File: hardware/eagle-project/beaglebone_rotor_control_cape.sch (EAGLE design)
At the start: 26 parts, among them IC1 TLC2264CDU, IC2 TLV5616, IC3 MAX3232ESE, Q1 SQ2348ES-T1-GE3, Q2 SQ2348ES-T1-GE3, X1 BEAGLEBONE_OUTLINE

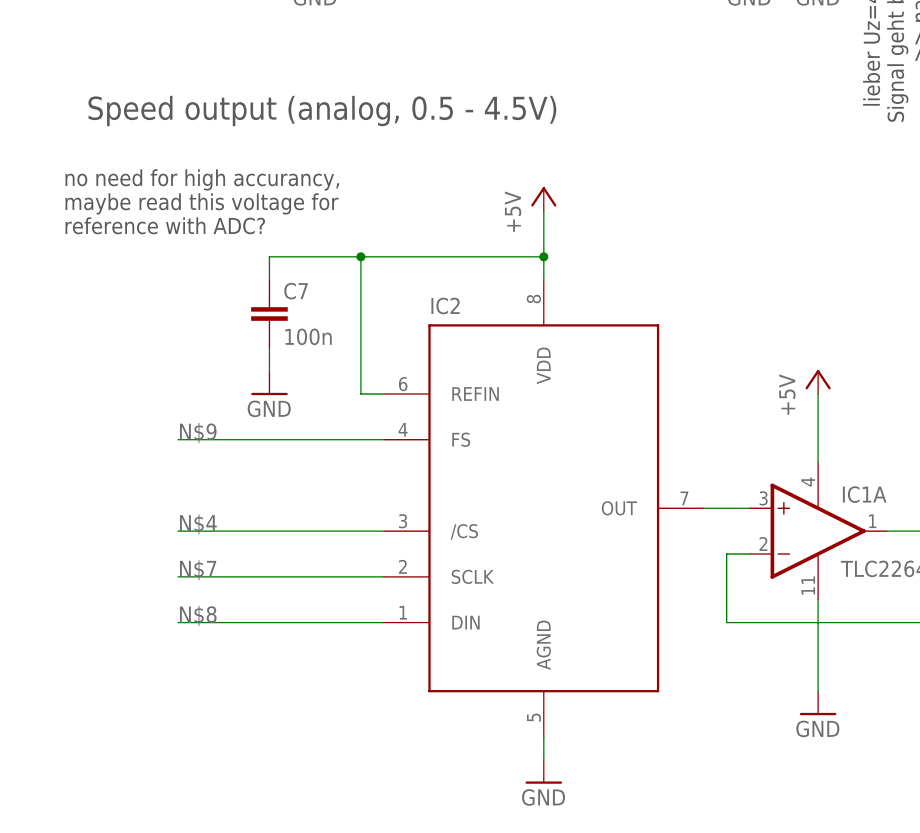
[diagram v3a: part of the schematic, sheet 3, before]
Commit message: Changed DAC from TI TLV5616 to Microchip MCP4901
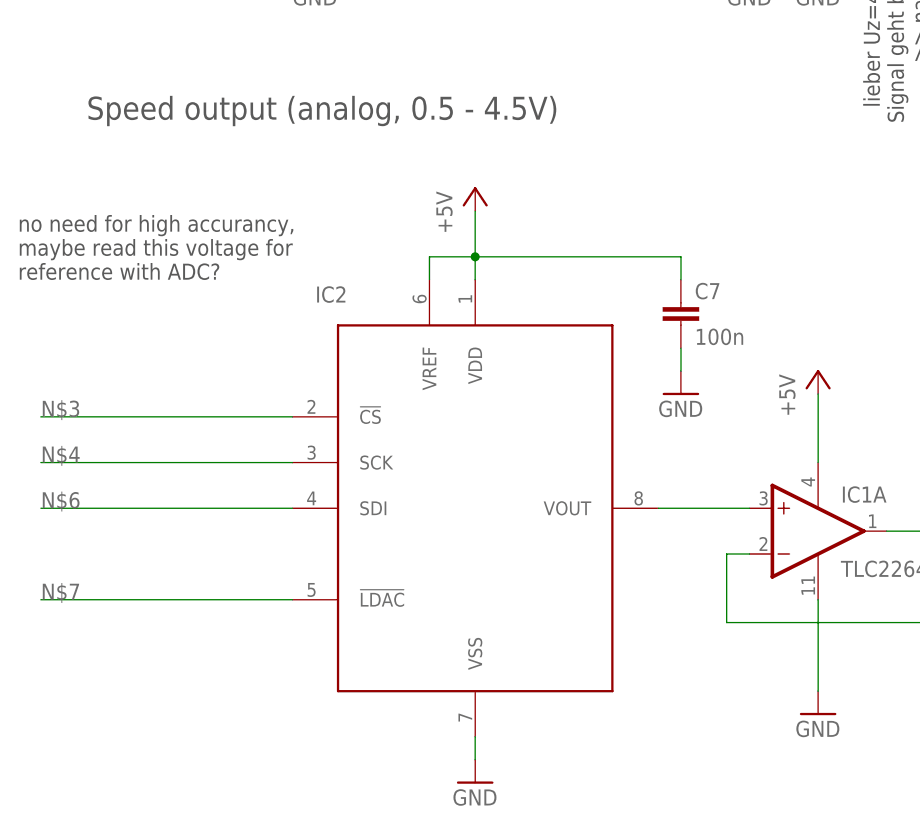
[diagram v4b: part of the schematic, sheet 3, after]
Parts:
- IC2: value TLV5616 -> MCP4901; device ti-tlv5616:TLV5616 -> microchip_mcp4901:MCP4901
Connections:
- removed net N$8: IC2.DIN
- removed net N$9: IC2.FS
- new net N$3: IC2.!CS
- new net N$6: IC2.SDI
- net +5V: now also IC2.VREF; no longer IC2.REFIN
- net GND: now also IC2.VSS; no longer IC2.AGND
- net N$2: now also IC2.VOUT; no longer IC2.OUT
- net N$4: now also IC2.SCK; no longer IC2./CS
- net N$7: now also IC2.!LDAC; no longer IC2.SCLK
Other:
- moved on the sheet: C7, IC2
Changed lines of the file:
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@@
 <part name="GND10" library="supply1" deviceset="GND" device=""/>
 <part name="P+1" library="supply1" deviceset="+5V" device=""/>
-<part name="IC2" library="ti-tlv5616" deviceset="TLV5616" device=""/>
 <part name="P+2" library="supply1" deviceset="+5V" device=""/>
 <part name="GND11" library="supply1" deviceset="GND" device=""/>
@@
 <part name="GND17" library="supply1" deviceset="GND" device=""/>
 <part name="GND18" library="supply1" deviceset="GND" device=""/>
+<part name="IC2" library="microchip_mcp4901" deviceset="MCP4901" device=""/>
 </parts>
 <sheets>
@@
 &gt;&gt; nachmessen!</text>
 <text x="76.2" y="116.84" size="1.778" layer="97">Vcc=5V</text>
-<text x="17.78" y="76.2" size="1.778" layer="97">no need for high accurancy,
+<text x="12.7" y="71.12" size="1.778" layer="97">no need for high accurancy,
 maybe read this voltage for
 reference with ADC?</text>
@@
 <instance part="GND10" gate="1" x="101.6" y="22.86"/>
 <instance part="P+1" gate="1" x="101.6" y="60.96"/>
-<instance part="IC2" gate="G$1" x="71.12" y="45.72"/>
-<instance part="P+2" gate="1" x="71.12" y="81.28"/>
-<instance part="GND11" gate="1" x="71.12" y="15.24"/>
+<instance part="P+2" gate="1" x="63.5" y="81.28"/>
+<instance part="GND11" gate="1" x="63.5" y="15.24"/>
 <instance part="IC1" gate="B" x="76.2" y="124.46" rot="R180"/>
 <instance part="R10" gate="G$1" x="111.76" y="121.92"/>
@@
 <instance part="R7" gate="G$1" x="177.8" y="96.52"/>
 <instance part="R6" gate="G$1" x="175.26" y="147.32"/>
-<instance part="C7" gate="G$1" x="40.64" y="68.58"/>
-<instance part="GND17" gate="1" x="40.64" y="58.42"/>
+<instance part="C7" gate="G$1" x="86.36" y="68.58"/>
+<instance part="GND17" gate="1" x="86.36" y="58.42"/>
 <instance part="GND18" gate="1" x="231.14" y="45.72"/>
+<instance part="IC2" gate="G$1" x="63.5" y="45.72"/>
 </instances>
 <busses>
@@
 </segment>
 <segment>
-<pinref part="IC2" gate="G$1" pin="AGND"/>
 <pinref part="GND11" gate="1" pin="GND"/>
-<wire x1="71.12" y1="17.78" x2="71.12" y2="20.32" width="0.1524" layer="91"/>
+<wire x1="63.5" y1="17.78" x2="63.5" y2="20.32" width="0.1524" layer="91"/>
+<pinref part="IC2" gate="G$1" pin="VSS"/>
 </segment>
 <segment>
@@
 <pinref part="C7" gate="G$1" pin="2"/>
 <pinref part="GND17" gate="1" pin="GND"/>
-<wire x1="40.64" y1="60.96" x2="40.64" y2="63.5" width="0.1524" layer="91"/>
+<wire x1="86.36" y1="60.96" x2="86.36" y2="63.5" width="0.1524" layer="91"/>
 </segment>
 </net>
@@
 </segment>
 <segment>
+<pinref part="P+2" gate="1" pin="+5V"/>
+<wire x1="63.5" y1="78.74" x2="63.5" y2="73.66" width="0.1524" layer="91"/>
+<pinref part="C7" gate="G$1" pin="1"/>
+<wire x1="63.5" y1="73.66" x2="63.5" y2="71.12" width="0.1524" layer="91"/>
+<wire x1="86.36" y1="71.12" x2="86.36" y2="73.66" width="0.1524" layer="91"/>
+<wire x1="86.36" y1="73.66" x2="63.5" y2="73.66" width="0.1524" layer="91"/>
+<junction x="63.5" y="73.66"/>
 <pinref part="IC2" gate="G$1" pin="VDD"/>
-<pinref part="P+2" gate="1" pin="+5V"/>
-<wire x1="71.12" y1="78.74" x2="71.12" y2="73.66" width="0.1524" layer="91"/>
-<pinref part="C7" gate="G$1" pin="1"/>
-<wire x1="71.12" y1="73.66" x2="71.12" y2="71.12" width="0.1524" layer="91"/>
-<wire x1="40.64" y1="71.12" x2="40.64" y2="73.66" width="0.1524" layer="91"/>
-<wire x1="40.64" y1="73.66" x2="50.8" y2="73.66" width="0.1524" layer="91"/>
-<junction x="71.12" y="73.66"/>
-<pinref part="IC2" gate="G$1" pin="REFIN"/>
-<wire x1="50.8" y1="73.66" x2="71.12" y2="73.66" width="0.1524" layer="91"/>
-<wire x1="53.34" y1="58.42" x2="50.8" y2="58.42" width="0.1524" layer="91"/>
-<wire x1="50.8" y1="58.42" x2="50.8" y2="73.66" width="0.1524" layer="91"/>
-<junction x="50.8" y="73.66"/>
+<pinref part="IC2" gate="G$1" pin="VREF"/>
+<wire x1="58.42" y1="71.12" x2="58.42" y2="73.66" width="0.1524" layer="91"/>
+<wire x1="58.42" y1="73.66" x2="63.5" y2="73.66" width="0.1524" layer="91"/>
 </segment>
 <segment>
@@
 <net name="N$2" class="0">
 <segment>
-<pinref part="IC2" gate="G$1" pin="OUT"/>
-<wire x1="88.9" y1="45.72" x2="93.98" y2="45.72" width="0.1524" layer="91"/>
+<wire x1="83.82" y1="45.72" x2="93.98" y2="45.72" width="0.1524" layer="91"/>
 <pinref part="IC1" gate="A" pin="+IN"/>
-</segment>
-</net>
-<net name="N$4" class="0">
-<segment>
-<pinref part="IC2" gate="G$1" pin="/CS"/>
-<wire x1="53.34" y1="43.18" x2="30.48" y2="43.18" width="0.1524" layer="91"/>
-<label x="30.48" y="43.18" size="1.778" layer="95"/>
-</segment>
-</net>
-<net name="N$7" class="0">
-<segment>
-<pinref part="IC2" gate="G$1" pin="SCLK"/>
-<wire x1="30.48" y1="38.1" x2="53.34" y2="38.1" width="0.1524" layer="91"/>
-<label x="30.48" y="38.1" size="1.778" layer="95"/>
-</segment>
-</net>
-<net name="N$8" class="0">
-<segment>
-<pinref part="IC2" gate="G$1" pin="DIN"/>
-<wire x1="53.34" y1="33.02" x2="30.48" y2="33.02" width="0.1524" layer="91"/>
-<label x="30.48" y="33.02" size="1.778" layer="95"/>
-</segment>
-</net>
-<net name="N$9" class="0">
-<segment>
-<pinref part="IC2" gate="G$1" pin="FS"/>
-<wire x1="53.34" y1="53.34" x2="30.48" y2="53.34" width="0.1524" layer="91"/>
-<label x="30.48" y="53.34" size="1.778" layer="95"/>
+<pinref part="IC2" gate="G$1" pin="VOUT"/>
 </segment>
 </net>
@@
 </segment>
 </net>
+<net name="N$3" class="0">
+<segment>
+<pinref part="IC2" gate="G$1" pin="!CS"/>
+<wire x1="43.18" y1="55.88" x2="15.24" y2="55.88" width="0.1524" layer="91"/>
+<label x="15.24" y="55.88" size="1.778" layer="95"/>
+</segment>
+</net>
+<net name="N$4" class="0">
+<segment>
+<pinref part="IC2" gate="G$1" pin="SCK"/>
+<wire x1="15.24" y1="50.8" x2="43.18" y2="50.8" width="0.1524" layer="91"/>
+<label x="15.24" y="50.8" size="1.778" layer="95"/>
+</segment>
+</net>
+<net name="N$6" class="0">
+<segment>
+<pinref part="IC2" gate="G$1" pin="SDI"/>
+<wire x1="43.18" y1="45.72" x2="15.24" y2="45.72" width="0.1524" layer="91"/>
+<label x="15.24" y="45.72" size="1.778" layer="95"/>
+</segment>
+</net>
+<net name="N$7" class="0">
+<segment>
+<pinref part="IC2" gate="G$1" pin="!LDAC"/>
+<wire x1="15.24" y1="35.56" x2="43.18" y2="35.56" width="0.1524" layer="91"/>
+<label x="15.24" y="35.56" size="1.778" layer="95"/>
+</segment>
+</net>

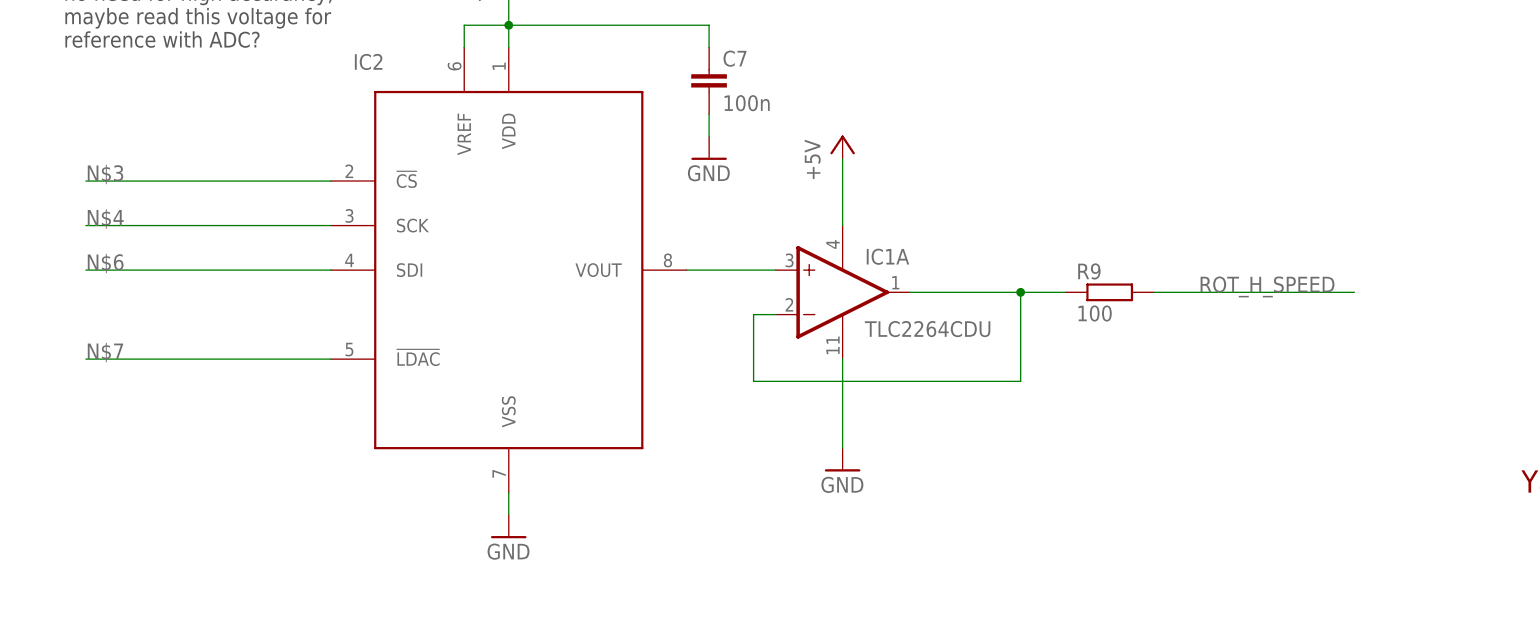
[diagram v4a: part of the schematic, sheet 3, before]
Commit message: Added software draft for MCP4901 and some Eagle schematic updates
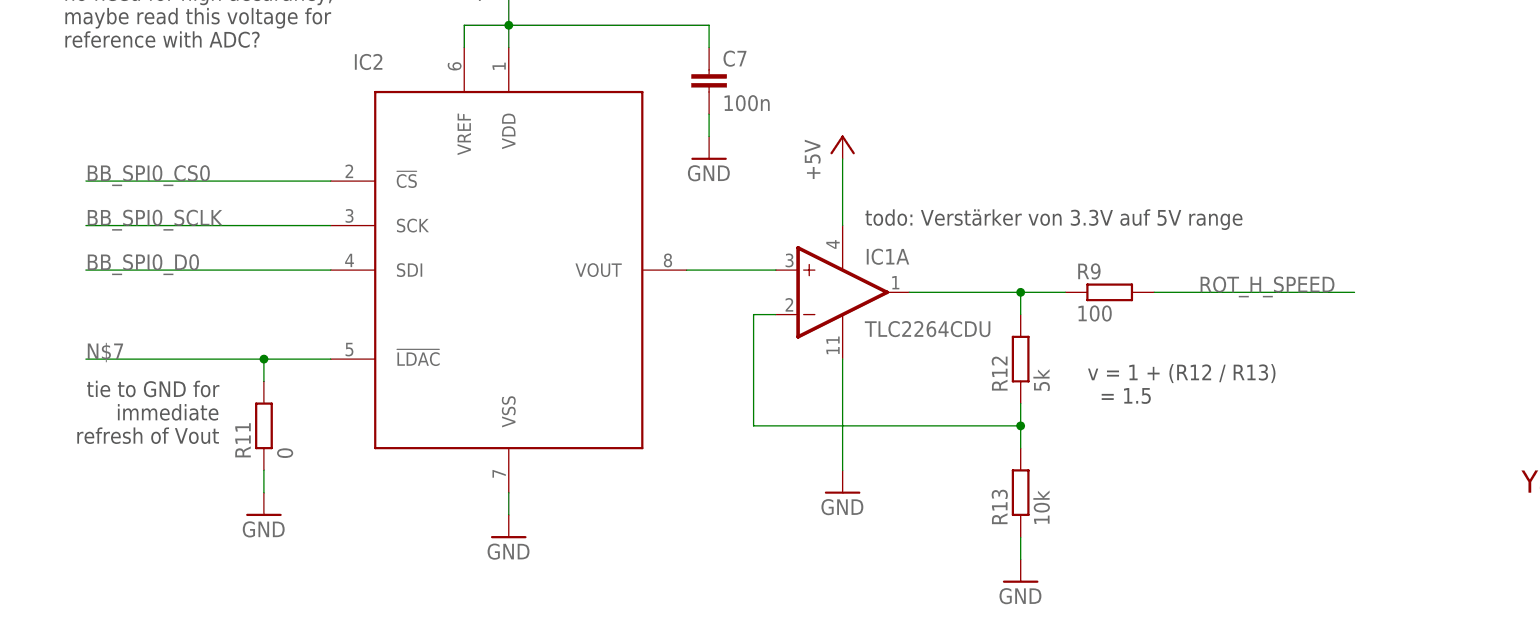
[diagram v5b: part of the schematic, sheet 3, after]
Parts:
- added R11: 0, rcl:R-EU_R0805
- added R12: 5k, rcl:R-EU_R0805
- added R13: 10k, rcl:R-EU_R0805
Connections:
- removed net N$4: IC2.SCK
- removed net N$6: IC2.SDI
- new net BB_SPI0_CS0: IC2.!CS, X1.I2C1_SCL
- new net BB_SPI0_D0: IC2.SDI, X1.UART2_TXD
- new net BB_SPI0_D1: X1.I2C1_SDA
- new net BB_SPI0_SCLK: IC2.SCK, X1.UART2_RXD
- net GND: now also R11.1, R13.1
- net N$3: now also IC1A.OUT, R12.2, R9.1; no longer IC2.!CS
- net N$5: now also R12.1, R13.2; no longer IC1A.OUT, R9.1
- net N$7: now also R11.2
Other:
- note added: "P9.11"
- note added: "P9.13"
- note added: "P9.17"
- note added: "P9.18"
- note added: "P9.21"
- note added: "P9.22"
- note added: "tie to GND for immediate refresh of Vout"
- note added: "todo: Verstärker von 3.3V auf 5V range"
- note added: "v = 1 + (R12 / R13) = 1.5"
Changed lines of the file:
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@@
 <part name="GND18" library="supply1" deviceset="GND" device=""/>
 <part name="IC2" library="microchip_mcp4901" deviceset="MCP4901" device=""/>
+<part name="R11" library="rcl" deviceset="R-EU_" device="R0805" value="0"/>
+<part name="GND19" library="supply1" deviceset="GND" device=""/>
+<part name="R12" library="rcl" deviceset="R-EU_" device="R0805" value="5k"/>
+<part name="R13" library="rcl" deviceset="R-EU_" device="R0805" value="10k"/>
+<part name="GND20" library="supply1" deviceset="GND" device=""/>
 </parts>
 <sheets>
@@
 <text x="147.32" y="152.4" size="2.54" layer="97">Information:</text>
 <text x="147.32" y="142.24" size="1.778" layer="97">- BeagleBone Black cape layout is provided by Adafruit</text>
+<text x="10.16" y="63.5" size="1.778" layer="97">P9.17</text>
+<text x="149.86" y="63.5" size="1.778" layer="97">P9.18</text>
+<text x="149.86" y="58.42" size="1.778" layer="97">P9.22</text>
+<text x="10.16" y="58.42" size="1.778" layer="97">P9.21</text>
+<text x="10.16" y="68.58" size="1.778" layer="97">P9.13</text>
+<text x="10.16" y="71.12" size="1.778" layer="97">P9.11</text>
 </plain>
 <instances>
@@
 <wire x1="22.86" y1="68.58" x2="53.34" y2="68.58" width="0.1524" layer="91"/>
 <label x="22.86" y="68.58" size="1.778" layer="95"/>
+</segment>
+</net>
+<net name="BB_SPI0_CS0" class="0">
+<segment>
+<pinref part="X1" gate="G$1" pin="I2C1_SCL"/>
+<wire x1="53.34" y1="63.5" x2="22.86" y2="63.5" width="0.1524" layer="91"/>
+<label x="22.86" y="63.5" size="1.778" layer="95"/>
+</segment>
+</net>
+<net name="BB_SPI0_D1" class="0">
+<segment>
+<pinref part="X1" gate="G$1" pin="I2C1_SDA"/>
+<wire x1="109.22" y1="63.5" x2="142.24" y2="63.5" width="0.1524" layer="91"/>
+<label x="119.38" y="63.5" size="1.778" layer="95"/>
+</segment>
+</net>
+<net name="BB_SPI0_D0" class="0">
+<segment>
+<pinref part="X1" gate="G$1" pin="UART2_TXD"/>
+<wire x1="53.34" y1="58.42" x2="22.86" y2="58.42" width="0.1524" layer="91"/>
+<label x="22.86" y="58.42" size="1.778" layer="95"/>
+</segment>
+</net>
+<net name="BB_SPI0_SCLK" class="0">
+<segment>
+<pinref part="X1" gate="G$1" pin="UART2_RXD"/>
+<wire x1="109.22" y1="58.42" x2="142.24" y2="58.42" width="0.1524" layer="91"/>
+<label x="119.38" y="58.42" size="1.778" layer="95"/>
 </segment>
 </net>
@@
 <text x="218.44" y="127" size="1.778" layer="97">wie open collector
 kurzschlussfest machen</text>
+<text x="104.14" y="50.8" size="1.778" layer="97">todo: Verstärker von 3.3V auf 5V range</text>
+<text x="30.48" y="33.02" size="1.778" layer="97" rot="R180">tie to GND for
+immediate
+refresh of Vout</text>
+<text x="129.54" y="30.48" size="1.778" layer="97">v = 1 + (R12 / R13)
+  = 1.5</text>
 </plain>
 <instances>
@@
 <instance part="IC1" gate="A" x="101.6" y="43.18"/>
 <instance part="IC1" gate="P" x="101.6" y="43.18"/>
-<instance part="GND10" gate="1" x="101.6" y="22.86"/>
+<instance part="GND10" gate="1" x="101.6" y="20.32"/>
 <instance part="P+1" gate="1" x="101.6" y="60.96"/>
 <instance part="P+2" gate="1" x="63.5" y="81.28"/>
@@
 <instance part="GND18" gate="1" x="231.14" y="45.72"/>
 <instance part="IC2" gate="G$1" x="63.5" y="45.72"/>
+<instance part="R11" gate="G$1" x="35.56" y="27.94" rot="R90"/>
+<instance part="GND19" gate="1" x="35.56" y="17.78"/>
+<instance part="R12" gate="G$1" x="121.92" y="35.56" rot="R90"/>
+<instance part="R13" gate="G$1" x="121.92" y="20.32" rot="R90"/>
+<instance part="GND20" gate="1" x="121.92" y="10.16"/>
 </instances>
 <busses>
@@
 <segment>
 <pinref part="IC1" gate="P" pin="V-"/>
-<wire x1="101.6" y1="35.56" x2="101.6" y2="25.4" width="0.1524" layer="91"/>
+<wire x1="101.6" y1="35.56" x2="101.6" y2="22.86" width="0.1524" layer="91"/>
 <pinref part="GND10" gate="1" pin="GND"/>
 </segment>
@@
 <pinref part="GND17" gate="1" pin="GND"/>
 <wire x1="86.36" y1="60.96" x2="86.36" y2="63.5" width="0.1524" layer="91"/>
+</segment>
+<segment>
+<pinref part="R11" gate="G$1" pin="1"/>
+<pinref part="GND19" gate="1" pin="GND"/>
+<wire x1="35.56" y1="20.32" x2="35.56" y2="22.86" width="0.1524" layer="91"/>
+</segment>
+<segment>
+<pinref part="R13" gate="G$1" pin="1"/>
+<pinref part="GND20" gate="1" pin="GND"/>
+<wire x1="121.92" y1="12.7" x2="121.92" y2="15.24" width="0.1524" layer="91"/>
 </segment>
 </net>
@@
 <net name="N$5" class="0">
 <segment>
-<pinref part="IC1" gate="A" pin="OUT"/>
-<wire x1="109.22" y1="43.18" x2="121.92" y2="43.18" width="0.1524" layer="91"/>
 <pinref part="IC1" gate="A" pin="-IN"/>
-<wire x1="121.92" y1="43.18" x2="127" y2="43.18" width="0.1524" layer="91"/>
 <wire x1="93.98" y1="40.64" x2="91.44" y2="40.64" width="0.1524" layer="91"/>
-<wire x1="91.44" y1="40.64" x2="91.44" y2="33.02" width="0.1524" layer="91"/>
-<wire x1="91.44" y1="33.02" x2="121.92" y2="33.02" width="0.1524" layer="91"/>
-<wire x1="121.92" y1="33.02" x2="121.92" y2="43.18" width="0.1524" layer="91"/>
-<junction x="121.92" y="43.18"/>
-<pinref part="R9" gate="G$1" pin="1"/>
+<wire x1="91.44" y1="40.64" x2="91.44" y2="27.94" width="0.1524" layer="91"/>
+<wire x1="91.44" y1="27.94" x2="121.92" y2="27.94" width="0.1524" layer="91"/>
+<pinref part="R12" gate="G$1" pin="1"/>
+<wire x1="121.92" y1="30.48" x2="121.92" y2="27.94" width="0.1524" layer="91"/>
+<pinref part="R13" gate="G$1" pin="2"/>
+<wire x1="121.92" y1="27.94" x2="121.92" y2="25.4" width="0.1524" layer="91"/>
+<junction x="121.92" y="27.94"/>
 </segment>
 </net>
@@
 </segment>
 </net>
-<net name="N$3" class="0">
+<net name="BB_SPI0_CS0" class="0">
 <segment>
 <pinref part="IC2" gate="G$1" pin="!CS"/>
@@
 </segment>
 </net>
-<net name="N$4" class="0">
+<net name="BB_SPI0_SCLK" class="0">
 <segment>
 <pinref part="IC2" gate="G$1" pin="SCK"/>
@@
 </segment>
 </net>
-<net name="N$6" class="0">
+<net name="BB_SPI0_D0" class="0">
 <segment>
 <pinref part="IC2" gate="G$1" pin="SDI"/>
@@
 <segment>
 <pinref part="IC2" gate="G$1" pin="!LDAC"/>
-<wire x1="15.24" y1="35.56" x2="43.18" y2="35.56" width="0.1524" layer="91"/>
+<wire x1="15.24" y1="35.56" x2="35.56" y2="35.56" width="0.1524" layer="91"/>
 <label x="15.24" y="35.56" size="1.778" layer="95"/>
-</segment>
-</net>
+<pinref part="R11" gate="G$1" pin="2"/>
+<wire x1="35.56" y1="35.56" x2="43.18" y2="35.56" width="0.1524" layer="91"/>
+<wire x1="35.56" y1="33.02" x2="35.56" y2="35.56" width="0.1524" layer="91"/>
+<junction x="35.56" y="35.56"/>
+</segment>
+</net>
+<net name="N$3" class="0">
+<segment>
+<pinref part="R9" gate="G$1" pin="1"/>
+<pinref part="IC1" gate="A" pin="OUT"/>
+<wire x1="109.22" y1="43.18" x2="121.92" y2="43.18" width="0.1524" layer="91"/>
+<pinref part="R12" gate="G$1" pin="2"/>
+<wire x1="121.92" y1="43.18" x2="127" y2="43.18" width="0.1524" layer="91"/>
+<wire x1="121.92" y1="43.18" x2="121.92" y2="40.64" width="0.1524" layer="91"/>
+<junction x="121.92" y="43.18"/>
+</segment>
+</net>
